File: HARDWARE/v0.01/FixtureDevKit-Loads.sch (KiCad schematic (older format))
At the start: 12 parts

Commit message: o gosh
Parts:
- removed J? (x3): LOAD_0, symbol Conn_01x03
- removed Q? (x3): Q_NMOS_GDSD, symbol Q_NMOS_GDSD
- removed R? (x3): 10R, 5W, symbol R
- added J?: LOAD_1, symbol Conn_01x03
- added J?: LOAD_2, symbol Conn_01x03
- added J?: LOAD_3, symbol Conn_01x03
- added Q? (x3): NTF2955T1G, symbol Q_NMOS_GDSD
- added R? (x3): 10R, 5W, symbol R
- added TP? (x4): S, symbol TEST
- added TP? (x4): G, symbol TEST
- added TP? (x4): D, symbol TEST
- Q?: value Q_NMOS_GDSD -> NTF2955T1G
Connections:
- net at R?.1: now also Q?.2 (D), Q?.4 (D); no longer J?.3 (Pin_3)
- net at J?.2 (Pin_2), Q?.1 (G): now also TP?.1
- net at J?.1 (Pin_1): now also R?.2, TP?.1; no longer Q?.3 (S)
- new net: J?.3 (Pin_3), Q?.3 (S), TP?.1 (x4)
- new net: Q?.2 (D), Q?.4 (D), R?.1 (x3)
- new net: J?.1 (Pin_1), R?.2, TP?.1 (x3)
- new net: J?.2 (Pin_2), Q?.1 (G), TP?.1 (x3)
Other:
- note added: "0.5"
- note added: "10"
- note added: "5"
- note added: "D->GND"
- note added: "G"
- note added: "LOAD_0\n"
- note added: "LOAD_1"
- note added: "LOAD_2"
- note added: "LOAD_3"
- note added: "Ohm's Law Cheat Sheet"
- note added: "P"
- note added: "R"
- note added: "V = C * R\nP = V * i"
- note added: "VS"
- note added: "V\n"
- note added: "i"
- note removed: "GND\n"
- note removed: "TRIGGER"
- note removed: "VCC"
- moved on the sheet: J?, Q?, R?

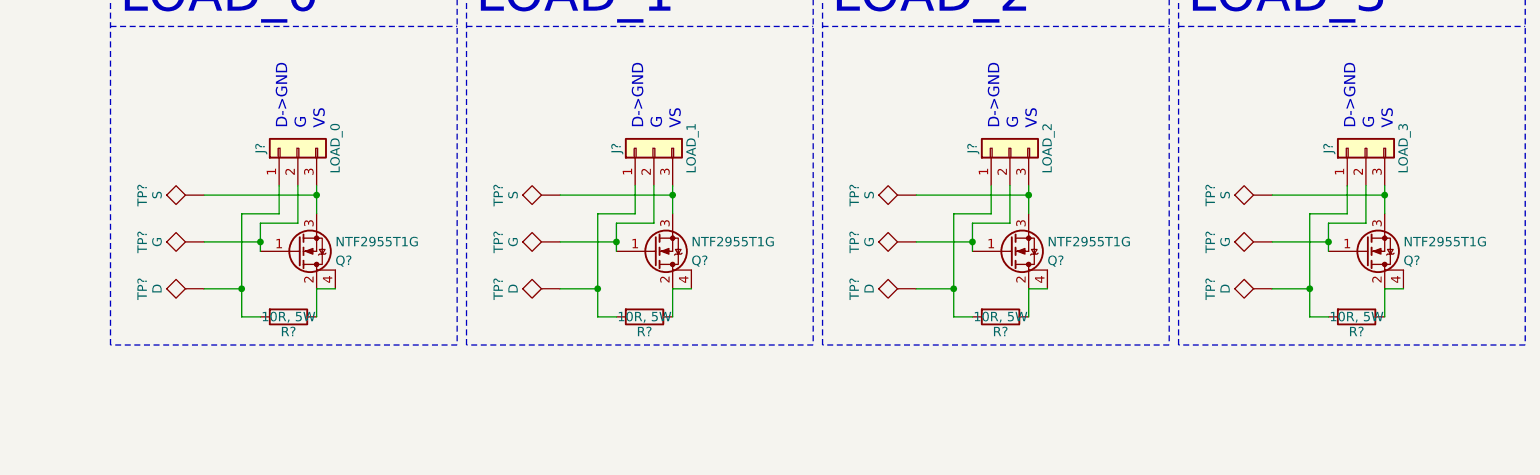
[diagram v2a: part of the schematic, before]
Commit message: adding netlist and design rules check
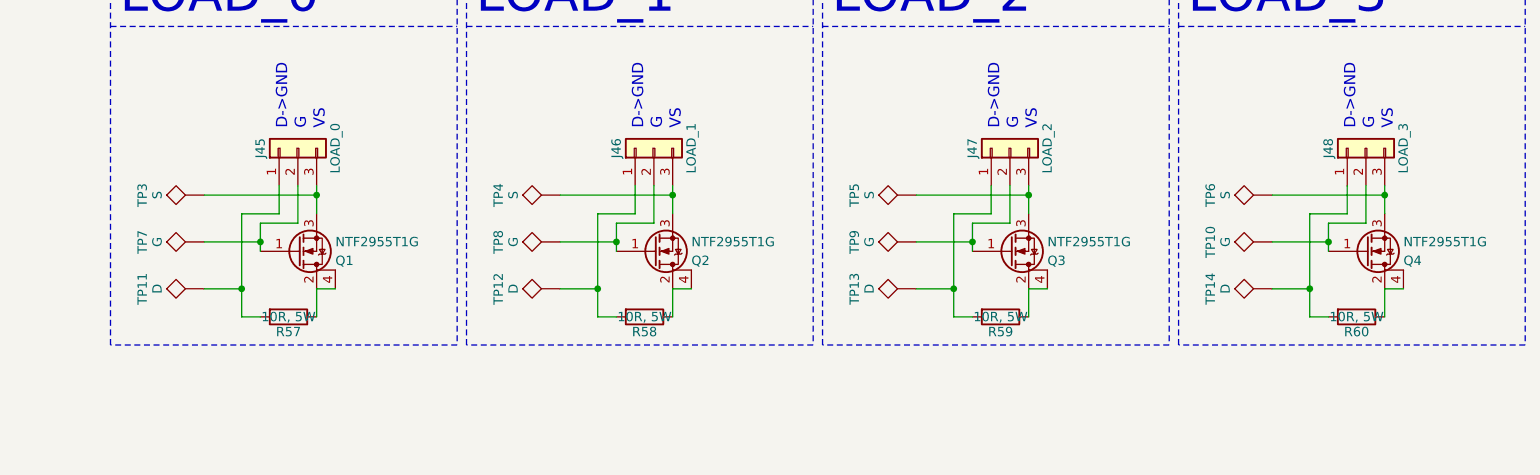
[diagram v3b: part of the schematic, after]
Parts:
- gave numbers to parts that had none: 24
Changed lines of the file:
@@
 VS
 $Comp
-L R R?
+L R R57
 U 1 1 59EE69C1
 P 3150 3800
-F 0 "R?" V 3230 3800 50  0000 C CNN
+F 0 "R57" V 3230 3800 50  0000 C CNN
 F 1 "10R, 5W" V 3150 3800 50  0000 C CNN
 F 2 "" V 3080 3800 50  0001 C CNN
@@
 $EndComp
 $Comp
-L Conn_01x03 J?
+L Conn_01x03 J45
 U 1 1 59EE6A91
 P 3200 2900
-F 0 "J?" H 3200 3100 50  0000 C CNN
+F 0 "J45" H 3200 3100 50  0000 C CNN
 F 1 "LOAD_0" H 3200 2700 50  0000 C CNN
 F 2 "" H 3200 2900 50  0001 C CNN
@@
 Dummy Load Circuit
 $Comp
-L Q_NMOS_GDSD Q?
+L Q_NMOS_GDSD Q1
 U 1 1 59EE6A15
 P 3200 3450
-F 0 "Q?" H 3400 3500 50  0000 L CNN
+F 0 "Q1" H 3400 3500 50  0000 L CNN
 F 1 "NTF2955T1G" H 3400 3400 50  0000 L CNN
 F 2 "" H 3400 3550 50  0001 C CNN
@@
 	3200 3300 3200 3100
 $Comp
-L TEST TP?
+L TEST TP3
 U 1 1 59F066A1
 P 2700 3150
-F 0 "TP?" H 2700 3450 50  0000 C BNN
+F 0 "TP3" H 2700 3450 50  0000 C BNN
 F 1 "S" H 2700 3400 50  0000 C CNN
 F 2 "" H 2700 3150 50  0001 C CNN
@@
 $EndComp
 $Comp
-L TEST TP?
+L TEST TP7
 U 1 1 59F06708
 P 2700 3400
-F 0 "TP?" H 2700 3700 50  0000 C BNN
+F 0 "TP7" H 2700 3700 50  0000 C BNN
 F 1 "G" H 2700 3650 50  0000 C CNN
 F 2 "" H 2700 3400 50  0001 C CNN
@@
 $EndComp
 $Comp
-L TEST TP?
+L TEST TP11
 U 1 1 59F0672F
 P 2700 3650
-F 0 "TP?" H 2700 3950 50  0000 C BNN
+F 0 "TP11" H 2700 3950 50  0000 C BNN
 F 1 "D" H 2700 3900 50  0000 C CNN
 F 2 "" H 2700 3650 50  0001 C CNN
@@
 VS
 $Comp
-L R R?
+L R R58
 U 1 1 59F074EB
 P 5050 3800
-F 0 "R?" V 5130 3800 50  0000 C CNN
+F 0 "R58" V 5130 3800 50  0000 C CNN
 F 1 "10R, 5W" V 5050 3800 50  0000 C CNN
 F 2 "" V 4980 3800 50  0001 C CNN
@@
 $EndComp
 $Comp
-L Conn_01x03 J?
+L Conn_01x03 J46
 U 1 1 59F074F1
 P 5100 2900
-F 0 "J?" H 5100 3100 50  0000 C CNN
+F 0 "J46" H 5100 3100 50  0000 C CNN
 F 1 "LOAD_1" H 5100 2700 50  0000 C CNN
 F 2 "" H 5100 2900 50  0001 C CNN
@@
 $EndComp
 $Comp
-L Q_NMOS_GDSD Q?
+L Q_NMOS_GDSD Q2
 U 1 1 59F074F7
 P 5100 3450
-F 0 "Q?" H 5300 3500 50  0000 L CNN
+F 0 "Q2" H 5300 3500 50  0000 L CNN
 F 1 "NTF2955T1G" H 5300 3400 50  0000 L CNN
 F 2 "" H 5300 3550 50  0001 C CNN
@@
 	5100 3300 5100 3100
 $Comp
-L TEST TP?
+L TEST TP4
 U 1 1 59F07507
 P 4600 3150
-F 0 "TP?" H 4600 3450 50  0000 C BNN
+F 0 "TP4" H 4600 3450 50  0000 C BNN
 F 1 "S" H 4600 3400 50  0000 C CNN
 F 2 "" H 4600 3150 50  0001 C CNN
@@
 $EndComp
 $Comp
-L TEST TP?
+L TEST TP8
 U 1 1 59F0750D
 P 4600 3400
-F 0 "TP?" H 4600 3700 50  0000 C BNN
+F 0 "TP8" H 4600 3700 50  0000 C BNN
 F 1 "G" H 4600 3650 50  0000 C CNN
 F 2 "" H 4600 3400 50  0001 C CNN
@@
 $EndComp
 $Comp
-L TEST TP?
+L TEST TP12
 U 1 1 59F07513
 P 4600 3650
-F 0 "TP?" H 4600 3950 50  0000 C BNN
+F 0 "TP12" H 4600 3950 50  0000 C BNN
 F 1 "D" H 4600 3900 50  0000 C CNN
 F 2 "" H 4600 3650 50  0001 C CNN
@@
 VS
 $Comp
-L R R?
+L R R59
 U 1 1 59F07D08
 P 6950 3800
-F 0 "R?" V 7030 3800 50  0000 C CNN
+F 0 "R59" V 7030 3800 50  0000 C CNN
 F 1 "10R, 5W" V 6950 3800 50  0000 C CNN
 F 2 "" V 6880 3800 50  0001 C CNN
@@
 $EndComp
 $Comp
-L Conn_01x03 J?
+L Conn_01x03 J47
 U 1 1 59F07D0E
 P 7000 2900
-F 0 "J?" H 7000 3100 50  0000 C CNN
+F 0 "J47" H 7000 3100 50  0000 C CNN
 F 1 "LOAD_2" H 7000 2700 50  0000 C CNN
 F 2 "" H 7000 2900 50  0001 C CNN
@@
 $EndComp
 $Comp
-L Q_NMOS_GDSD Q?
+L Q_NMOS_GDSD Q3
 U 1 1 59F07D14
 P 7000 3450
-F 0 "Q?" H 7200 3500 50  0000 L CNN
+F 0 "Q3" H 7200 3500 50  0000 L CNN
 F 1 "NTF2955T1G" H 7200 3400 50  0000 L CNN
 F 2 "" H 7200 3550 50  0001 C CNN
@@
 	7000 3300 7000 3100
 $Comp
-L TEST TP?
+L TEST TP5
 U 1 1 59F07D24
 P 6500 3150
-F 0 "TP?" H 6500 3450 50  0000 C BNN
+F 0 "TP5" H 6500 3450 50  0000 C BNN
 F 1 "S" H 6500 3400 50  0000 C CNN
 F 2 "" H 6500 3150 50  0001 C CNN
@@
 $EndComp
 $Comp
-L TEST TP?
+L TEST TP9
 U 1 1 59F07D2A
 P 6500 3400
-F 0 "TP?" H 6500 3700 50  0000 C BNN
+F 0 "TP9" H 6500 3700 50  0000 C BNN
 F 1 "G" H 6500 3650 50  0000 C CNN
 F 2 "" H 6500 3400 50  0001 C CNN
@@
 $EndComp
 $Comp
-L TEST TP?
+L TEST TP13
 U 1 1 59F07D30
 P 6500 3650
-F 0 "TP?" H 6500 3950 50  0000 C BNN
+F 0 "TP13" H 6500 3950 50  0000 C BNN
 F 1 "D" H 6500 3900 50  0000 C CNN
 F 2 "" H 6500 3650 50  0001 C CNN
@@
 VS
 $Comp
-L R R?
+L R R60
 U 1 1 59F07D45
 P 8850 3800
-F 0 "R?" V 8930 3800 50  0000 C CNN
+F 0 "R60" V 8930 3800 50  0000 C CNN
 F 1 "10R, 5W" V 8850 3800 50  0000 C CNN
 F 2 "" V 8780 3800 50  0001 C CNN
@@
 $EndComp
 $Comp
-L Conn_01x03 J?
+L Conn_01x03 J48
 U 1 1 59F07D4B
 P 8900 2900
-F 0 "J?" H 8900 3100 50  0000 C CNN
+F 0 "J48" H 8900 3100 50  0000 C CNN
 F 1 "LOAD_3" H 8900 2700 50  0000 C CNN
 F 2 "" H 8900 2900 50  0001 C CNN
@@
 $EndComp
 $Comp
-L Q_NMOS_GDSD Q?
+L Q_NMOS_GDSD Q4
 U 1 1 59F07D51
 P 8900 3450
-F 0 "Q?" H 9100 3500 50  0000 L CNN
+F 0 "Q4" H 9100 3500 50  0000 L CNN
 F 1 "NTF2955T1G" H 9100 3400 50  0000 L CNN
 F 2 "" H 9100 3550 50  0001 C CNN
@@
 	8900 3300 8900 3100
 $Comp
-L TEST TP?
+L TEST TP6
 U 1 1 59F07D61
 P 8400 3150
-F 0 "TP?" H 8400 3450 50  0000 C BNN
+F 0 "TP6" H 8400 3450 50  0000 C BNN
 F 1 "S" H 8400 3400 50  0000 C CNN
 F 2 "" H 8400 3150 50  0001 C CNN
@@
 $EndComp
 $Comp
-L TEST TP?
+L TEST TP10
 U 1 1 59F07D67
 P 8400 3400
-F 0 "TP?" H 8400 3700 50  0000 C BNN
+F 0 "TP10" H 8400 3700 50  0000 C BNN
 F 1 "G" H 8400 3650 50  0000 C CNN
 F 2 "" H 8400 3400 50  0001 C CNN
@@
 $EndComp
 $Comp
-L TEST TP?
+L TEST TP14
 U 1 1 59F07D6D
 P 8400 3650
-F 0 "TP?" H 8400 3950 50  0000 C BNN
+F 0 "TP14" H 8400 3950 50  0000 C BNN
 F 1 "D" H 8400 3900 50  0000 C CNN
 F 2 "" H 8400 3650 50  0001 C CNN
